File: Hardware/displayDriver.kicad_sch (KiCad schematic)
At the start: 22 parts, among them J3 Conn_01x10, J4 Conn_01x10, U10 4511, U11 HDSP-816E, U12 4511, U13 HDSP-816E, U6 4511, U7 HDSP-816E, U8 4511, U9 HDSP-816E

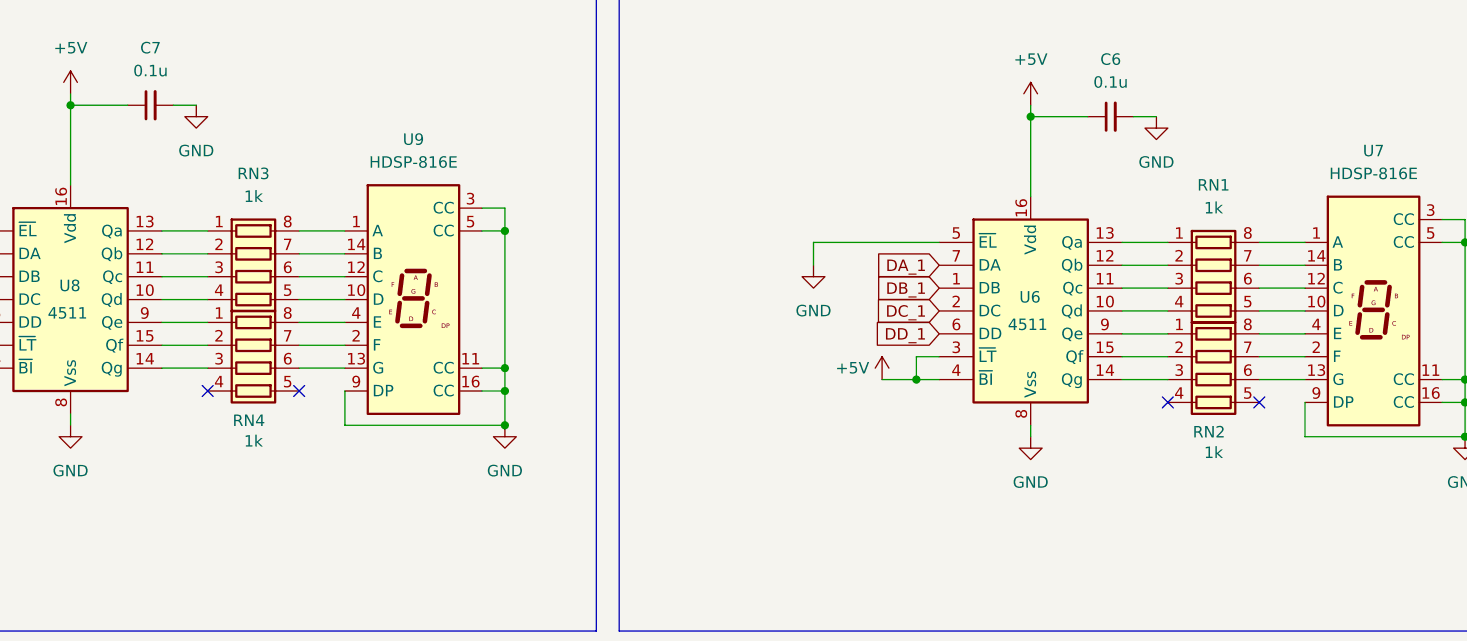
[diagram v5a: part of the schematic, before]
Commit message: Adjust minutes resistor packs to make them flow better
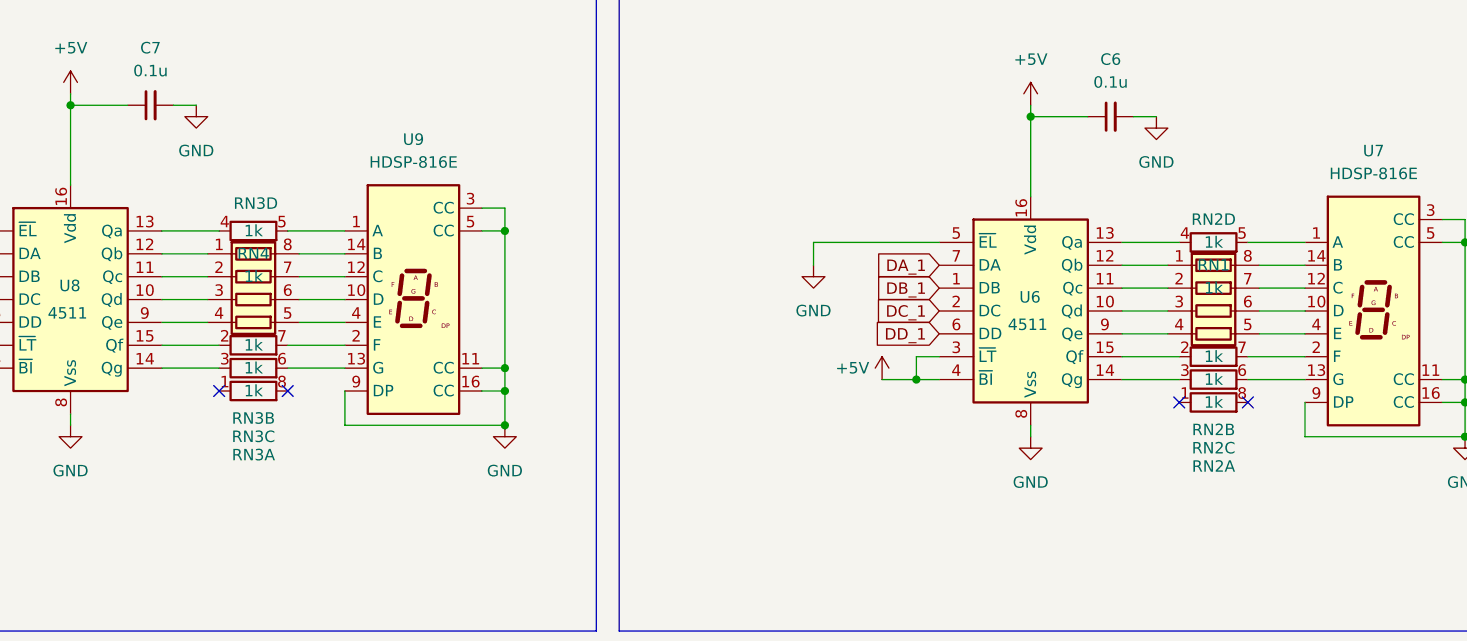
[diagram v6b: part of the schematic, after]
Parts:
- removed RN2, RN3: 1k, Resistor_SMD:R_Array_Convex_4x0603, symbol Device:R_Pack04
- added RN2, RN3: 1k, Resistor_SMD:R_Array_Convex_4x0603, symbol Device:R_Pack04_Split
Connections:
- net at U6.9 (Qe): now also RN1.4 (R4.1)
- net at U6.15 (Qf): now also RN2.2 (R2.1)
- net at U6.14 (Qg): now also RN2.3 (R3.1)
- net at U7.13 (G): now also RN2.6 (R3.2)
- net at U7.2 (F): now also RN2.7 (R2.2)
- net at U7.4 (E): now also RN1.5 (R4.2)
- net at U6.10 (Qd): now also RN1.3 (R3.1); no longer RN1.4 (R4.1)
- net at U6.11 (Qc): now also RN1.2 (R2.1); no longer RN1.3 (R3.1)
- net at U6.12 (Qb): now also RN1.1 (R1.1); no longer RN1.2 (R2.1)
- net at U6.13 (Qa): now also RN2.4 (R4.1); no longer RN1.1 (R1.1)
- net at RN4.1 (R1.1): now also U8.12 (Qb); no longer U8.9 (Qe)
- net at U8.15 (Qf): now also RN3.2 (R2.1); no longer RN4.2 (R2.1)
- net at U8.14 (Qg): now also RN3.3 (R3.1); no longer RN4.3 (R3.1)
- net at RN4.4 (R4.1): now also U8.9 (Qe)
- net at RN4.5 (R4.2): now also U9.4 (E)
- net at U9.13 (G): now also RN3.6 (R3.2); no longer RN4.6 (R3.2)
- net at U9.2 (F): now also RN3.7 (R2.2); no longer RN4.7 (R2.2)
- net at RN4.8 (R1.2): now also U9.14 (B); no longer U9.4 (E)
- net at U8.10 (Qd): now also RN4.3 (R3.1)
- net at U8.11 (Qc): now also RN4.2 (R2.1)
- net at U8.13 (Qa): now also RN3.4 (R4.1)
- net at RN1.8 (R1.2): now also U7.14 (B); no longer U7.1 (A)
- net at U7.10 (D): now also RN1.6 (R3.2); no longer RN1.5 (R4.2)
- net at U7.12 (C): now also RN1.7 (R2.2); no longer RN1.6 (R3.2)
- net at U9.1 (A): now also RN3.5 (R4.2)
- net at U9.10 (D): now also RN4.6 (R3.2)
- net at U9.12 (C): now also RN4.7 (R2.2)
- new net: RN2.5 (R4.2), U7.1 (A)

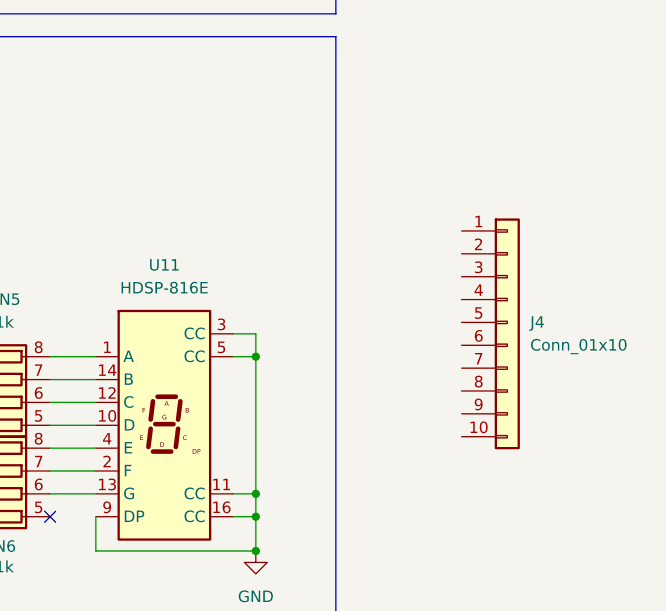
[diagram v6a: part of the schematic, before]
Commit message: Wire up the Hours connectors
Signed-off-by: Joel Cranmer <42.joel.cranmer@gmail.com>
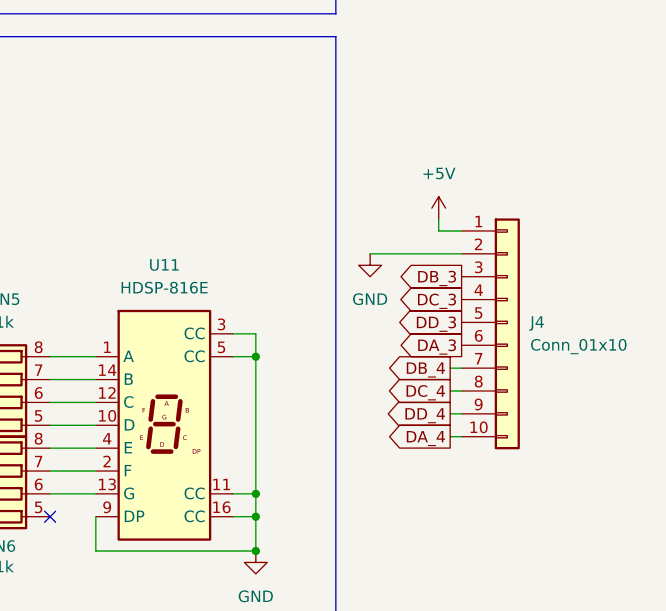
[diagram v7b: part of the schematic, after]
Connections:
- net +5V: now also J4.1 (Pin_1)
- net DA_3: now also J4.6 (Pin_6)
- net DA_4: now also J4.10 (Pin_10)
- net DB_3: now also J4.3 (Pin_3)
- net DB_4: now also J4.7 (Pin_7)
- net DC_3: now also J4.4 (Pin_4)
- net DC_4: now also J4.8 (Pin_8)
- net DD_3: now also J4.5 (Pin_5)
- net DD_4: now also J4.9 (Pin_9)
- net GND: now also J4.2 (Pin_2)

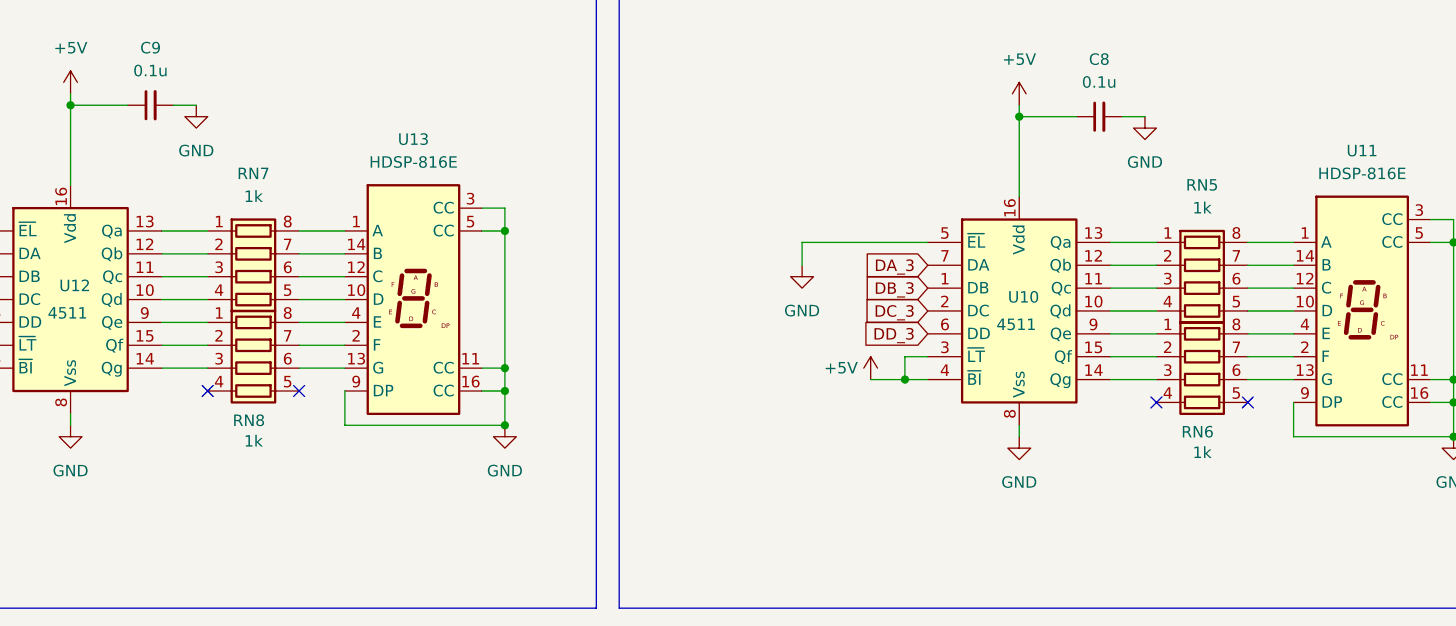
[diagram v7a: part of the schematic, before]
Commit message: Fix resistor arrays for more logical layout
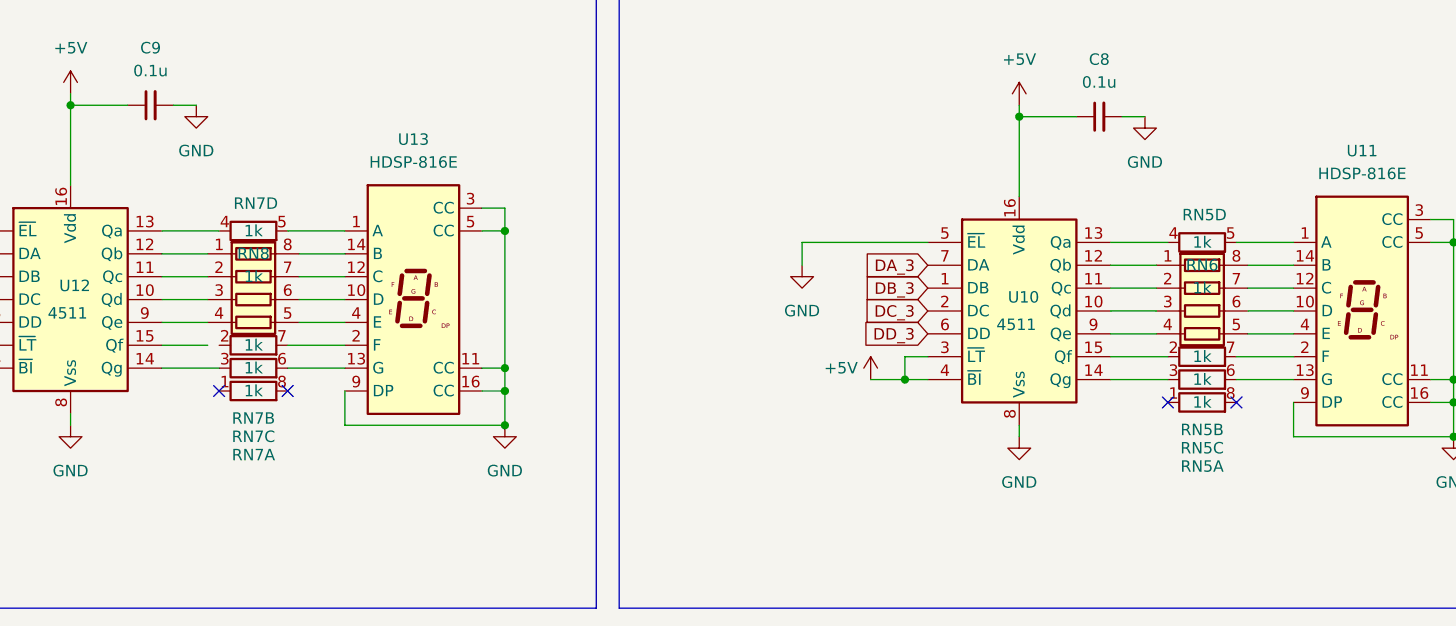
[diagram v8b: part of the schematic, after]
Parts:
- removed RN5, RN7: 1k, Resistor_SMD:R_Array_Convex_4x0603, symbol Device:R_Pack04
- added RN5, RN7: 1k, Resistor_SMD:R_Array_Convex_4x0603, symbol Device:R_Pack04_Split
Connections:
- net at U12.13 (Qa): now also RN7.4 (R4.1)
- net at U12.12 (Qb): now also RN8.1 (R1.1)
- net at U12.11 (Qc): now also RN8.2 (R2.1)
- net at U12.10 (Qd): now also RN8.3 (R3.1)
- net at U13.10 (D): now also RN8.6 (R3.2)
- net at U13.12 (C): now also RN8.7 (R2.2)
- net at U13.14 (B): now also RN8.8 (R1.2)
- net at U13.1 (A): now also RN7.5 (R4.2)
- net at U13.13 (G): now also RN7.6 (R3.2); no longer RN8.6 (R3.2)
- net at U13.2 (F): now also RN7.7 (R2.2); no longer RN8.7 (R2.2)
- net at U13.4 (E): now also RN8.5 (R4.2); no longer RN8.8 (R1.2)
- net at U12.9 (Qe): now also RN8.4 (R4.1); no longer RN8.1 (R1.1)
- net at U12.15 (Qf): no longer RN8.2 (R2.1)
- net at U12.14 (Qg): now also RN7.3 (R3.1); no longer RN8.3 (R3.1)
- net at RN6.1 (R1.1): now also U10.12 (Qb); no longer U10.9 (Qe)
- net at RN6.2 (R2.1): now also U10.11 (Qc); no longer U10.15 (Qf)
- net at U10.14 (Qg): now also RN5.3 (R3.1); no longer RN6.3 (R3.1)
- net at RN6.4 (R4.1): now also U10.9 (Qe)
- net at RN6.5 (R4.2): now also U11.4 (E)
- net at U11.13 (G): now also RN5.6 (R3.2); no longer RN6.6 (R3.2)
- net at RN6.7 (R2.2): now also U11.12 (C); no longer U11.2 (F)
- net at RN6.8 (R1.2): now also U11.14 (B); no longer U11.4 (E)
- net at U11.1 (A): now also RN5.5 (R4.2)
- net at U11.10 (D): now also RN6.6 (R3.2)
- net at U10.13 (Qa): now also RN5.4 (R4.1)
- net at U10.10 (Qd): now also RN6.3 (R3.1)
- new net: RN5.2 (R2.1), U10.15 (Qf)
- new net: RN5.7 (R2.2), U11.2 (F)
